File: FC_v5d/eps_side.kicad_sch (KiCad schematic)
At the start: 67 parts, among them IC6 LT3652IMSE#PBF, J10 INHIBIT_P2, J11 DF11CZ-12DP-2V(27), J14 Battery Input, J17 Face4 (Z- Face), J19 ISS_INHIBIT, J2 DF11CZ-12DP-2V(27), J20 RBF_Inhibit, J21 Heater Output, J23 Aux Deploy 1, J24 Deploy 2, J29 INHIBIT_S2, J7 INHIBIT_P1, J8 INHIBIT_S1, U10 TPS54226PWPRPWP14_2P31X2P46-L, U13 TPS54225PWPR, U26 INA260, U3 INA260, U9 MCP23017_SS

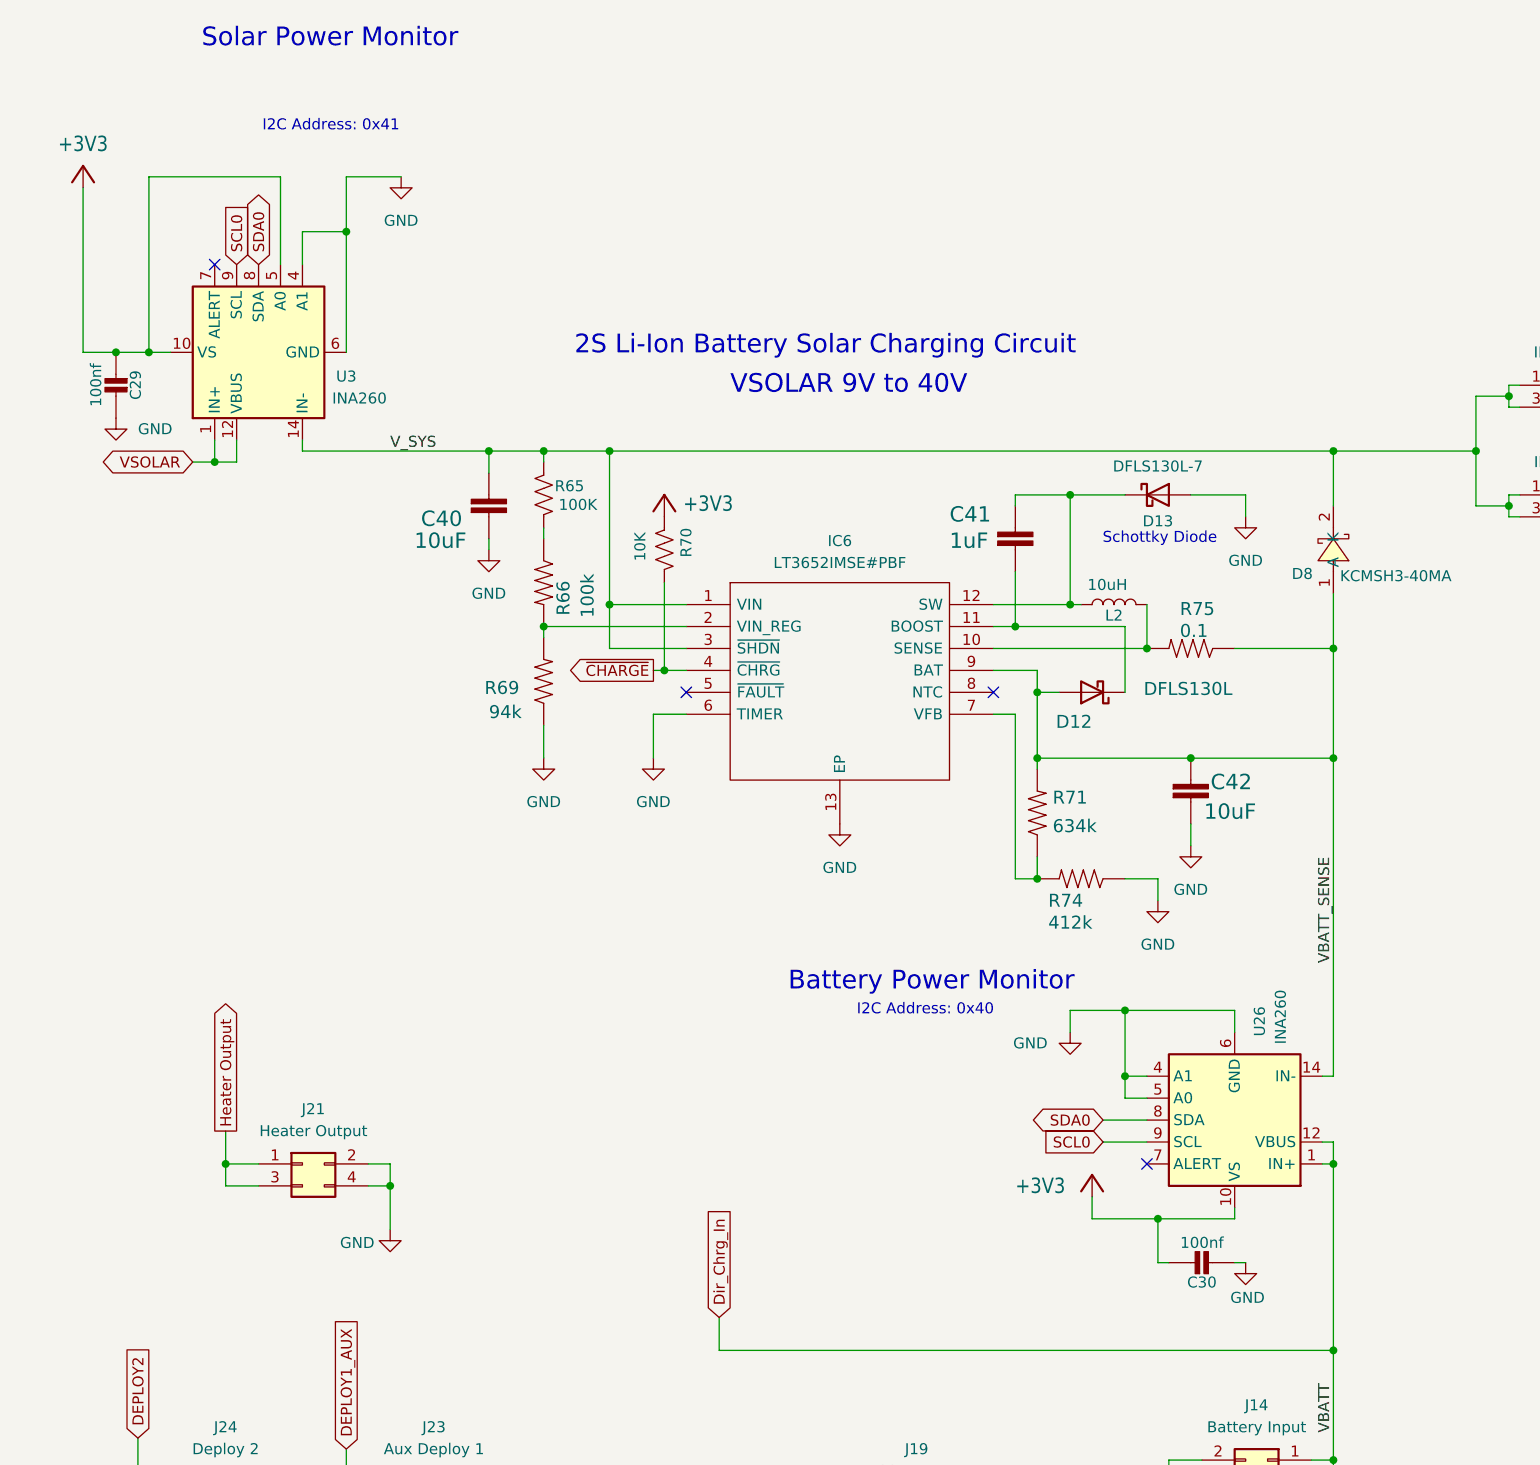
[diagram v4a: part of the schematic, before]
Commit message: Switched Back to INA219 Power Monitors
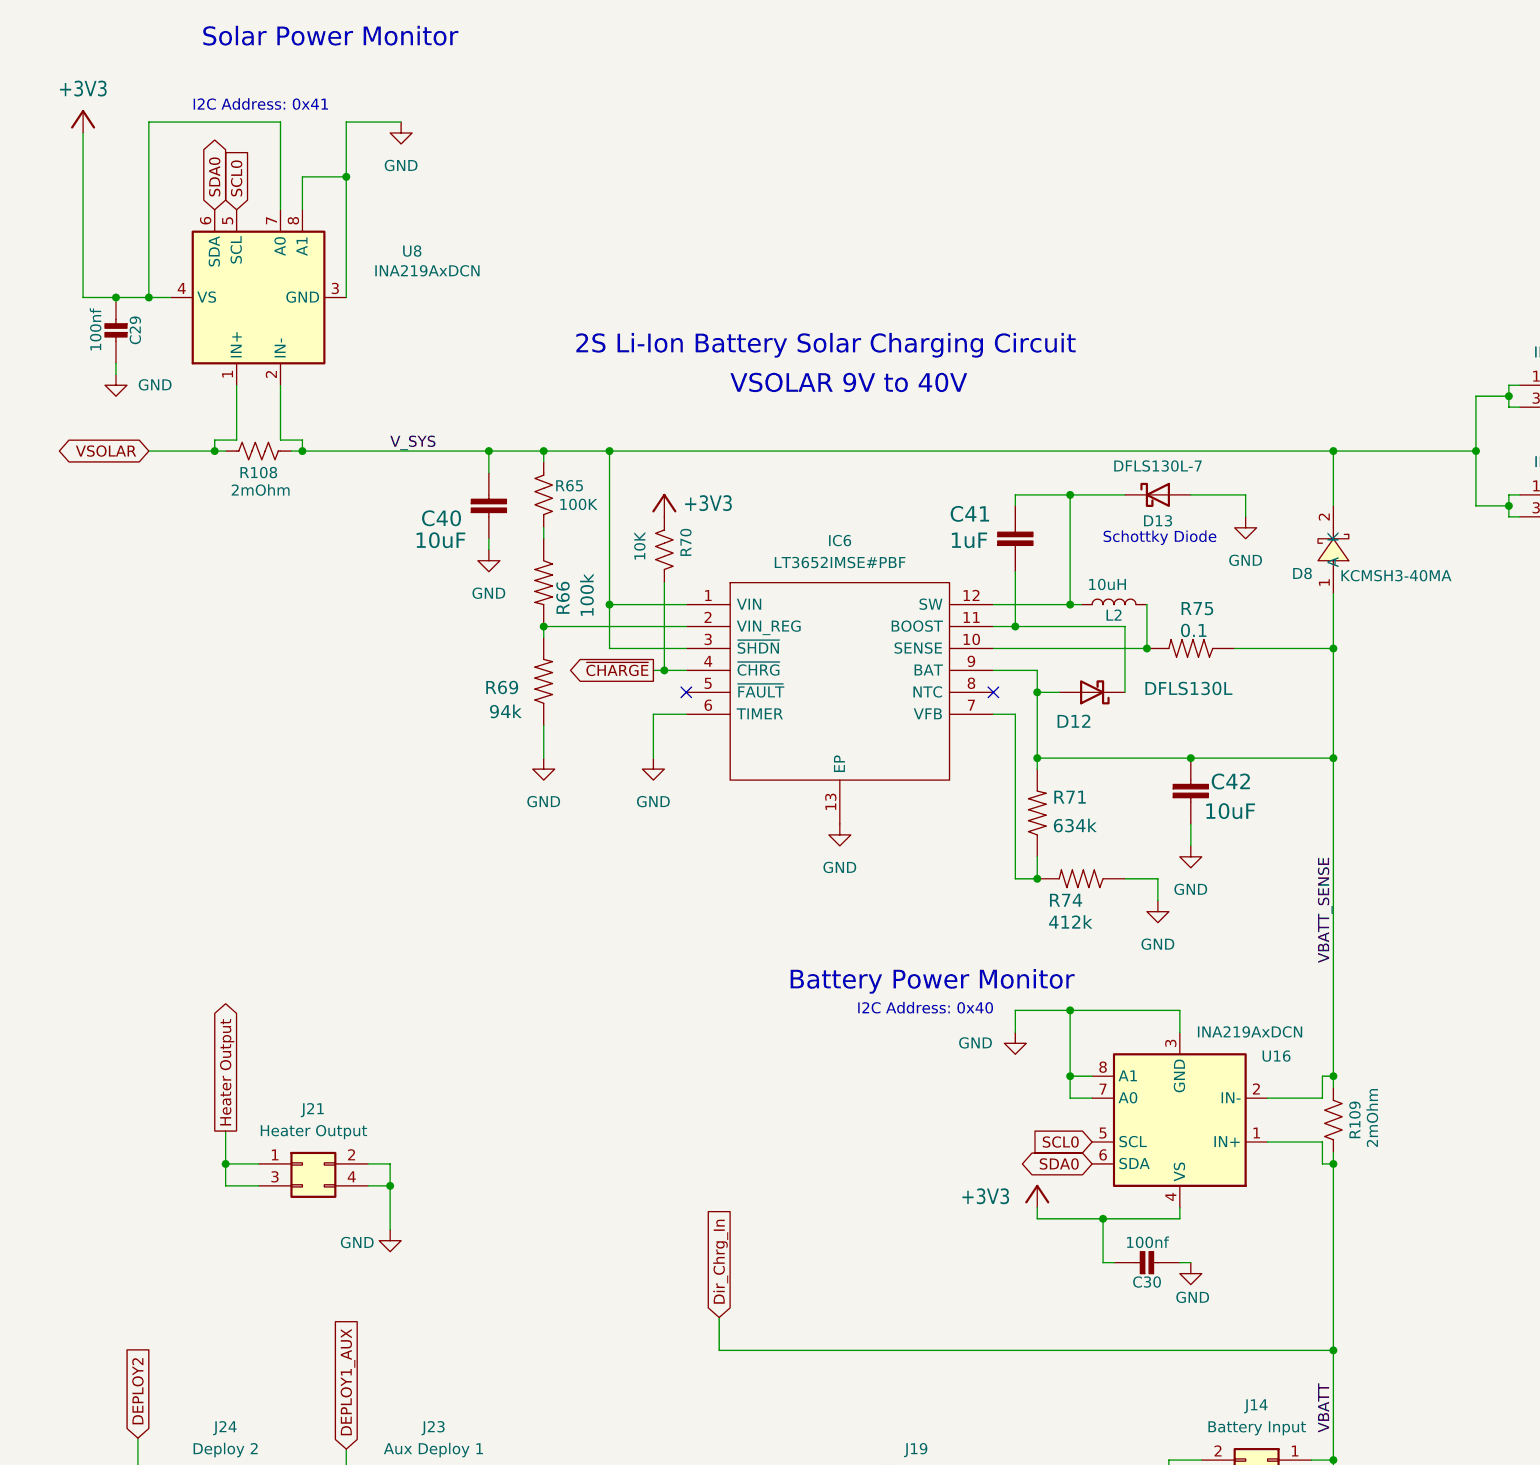
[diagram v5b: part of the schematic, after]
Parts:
- removed U26, U3: INA260, Package_SO:TSSOP-16_4.4x5mm_P0.65mm, symbol Sensor:INA260
- added R108, R109: 2mOhm, LED_SMD:LED_1210_3225Metric, symbol Device:R_US
- added U16, U8: INA219AxDCN, Package_TO_SOT_SMD:SOT-23-8, symbol Sensor_Energy:INA219AxDCN
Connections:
- net +3V3: now also U16.4 (VS), U8.4 (VS), U8.7 (A0)
- net Dir_Chrg_In: now also R109.1, U16.1 (IN+)
- net GND: now also U16.3 (GND), U16.7 (A0), U16.8 (A1), U8.3 (GND), U8.8 (A1)
- net SCL0: now also U16.5 (SCL), U8.5 (SCL)
- net SDA0: now also U16.6 (SDA), U8.6 (SDA)
- net VBATT_SENSE: now also R109.2, U16.2 (IN-)
- net VSOLAR: now also R108.1, U8.1 (IN+)
- net V_SYS: now also R108.2, U8.2 (IN-)
- no-connect marks 10 -> 8
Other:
- moved on the sheet: C29, C30
